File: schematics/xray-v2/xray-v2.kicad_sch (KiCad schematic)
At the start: 136 parts, among them J1 USB_B_Micro, J2 USB_A, J3 USB_C_Receptacle_USB2.0, J4 USBASP, M1 VibroMotor, 3V, 8x2.7mm, Q1 IRF7832PbF, Q10 IRLML5203, Q11 IRLML0030, Q12 IRLML0030, Q13 IRLML0030, Q14 IRLML0030, Q2 IRF7425PbF, Q3 IRLML0030, Q4 IRF7425PbF, Q7 BC847, Q8 IRLML0030, Q9 IRLML5203, SW1 EC11W****, SW2 B3F3150, SW3 SW_Push, T1 Transformer_1P_1S, U1 PCA9306, U2 IP5328P, U3 ATmega328P-A, U4 SN74LVC2T45DCUR, U5 SN74LVC2T45DCUR, U6 SN74LVC2T45DCUR, U7 Display_1.18inch_st7535, U8 AMS1117-3.3, U9 CP2102N-Axx-xQFN28, Y1 HC-49SM, 8MHz

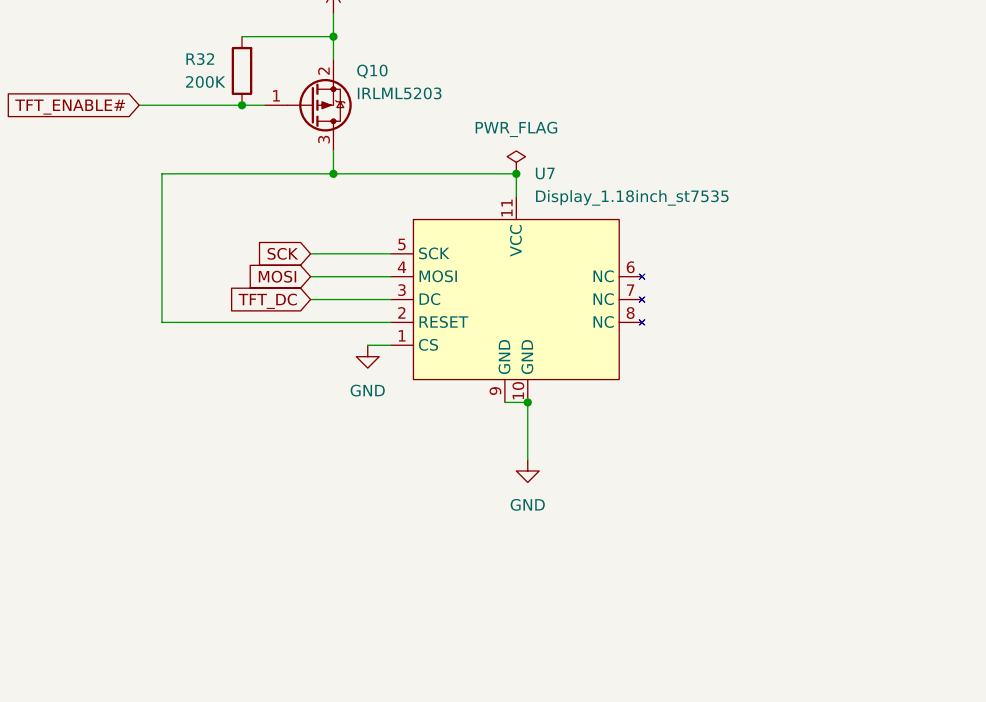
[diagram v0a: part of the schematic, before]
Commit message: Display changed 1.8'' -> 2.2''
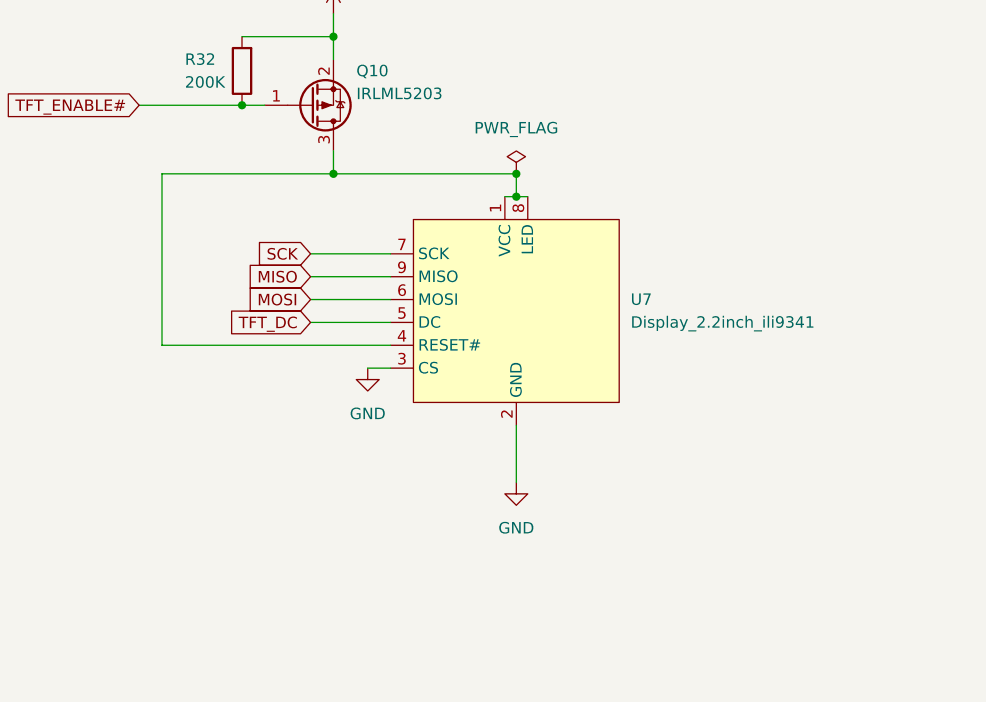
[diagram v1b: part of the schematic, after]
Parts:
- removed U7: Display_1.18inch_st7535, Library:Display_1.18inch_st7735, symbol My_Library:Display_1.18inch_st7535
- added U7: Display_2.2inch_ili9341, Library:Display_2.2inch_ili9341, symbol My_Library:Display_2.2inch_ili9341
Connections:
- net GND: now also U7.2 (GND), U7.3 (CS)
- net MISO: now also U7.9 (MISO)
- net MOSI: now also U7.6 (MOSI)
- net SCK: now also U7.7 (SCK)
- net TFT_DC: now also U7.5 (DC)
- net at Q10.3 (D): now also U7.1 (VCC), U7.4 (RESET#), U7.8 (LED)
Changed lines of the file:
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@@
   (junction (at 71.12 99.06) (diameter 0) (color 0 0 0 0)
   )
+  (junction (at 763.27 393.7) (diameter 0) (color 0 0 0 0)
+  )
   (junction (at 685.8 247.65) (diameter 0) (color 0 0 0 0)
   )
@@
   (junction (at 149.86 494.03) (diameter 0) (color 0 0 0 0)
   )
-  (junction (at 764.54 416.56) (diameter 0) (color 0 0 0 0)
-  )
   (junction (at 445.77 293.37) (diameter 0) (color 0 0 0 0)
   )
@@
     (stroke (width 0) (type default))
   )
-  (wire (pts (xy 749.3 405.13) (xy 740.41 405.13))
+  (wire (pts (xy 749.3 407.67) (xy 740.41 407.67))
     (stroke (width 0) (type default))
   )
@@
     (stroke (width 0) (type default))
   )
-  (wire (pts (xy 762 416.56) (xy 764.54 416.56))
-    (stroke (width 0) (type default))
-  )
   (wire (pts (xy 306.07 121.92) (xy 318.77 121.92))
     (stroke (width 0) (type default))
@@
     (stroke (width 0) (type default))
   )
-  (wire (pts (xy 764.54 416.56) (xy 764.54 422.91))
+  (wire (pts (xy 763.27 419.1) (xy 763.27 425.45))
     (stroke (width 0) (type default))
   )
@@
     (stroke (width 0) (type default))
   )
-  (wire (pts (xy 749.3 402.59) (xy 740.41 402.59))
+  (wire (pts (xy 749.3 405.13) (xy 740.41 405.13))
     (stroke (width 0) (type default))
   )
@@
     (stroke (width 0) (type default))
   )
+  (wire (pts (xy 763.27 393.7) (xy 764.54 393.7))
+    (stroke (width 0) (type default))
+  )
   (wire (pts (xy 659.13 241.3) (xy 659.13 247.65))
     (stroke (width 0) (type default))
@@
     (stroke (width 0) (type default))
   )
-  (wire (pts (xy 723.9 407.67) (xy 749.3 407.67))
-    (stroke (width 0) (type default))
-  )
   (wire (pts (xy 71.12 106.68) (xy 71.12 107.95))
     (stroke (width 0) (type default))
@@
     (stroke (width 0) (type default))
   )
+  (wire (pts (xy 749.3 402.59) (xy 740.41 402.59))
+    (stroke (width 0) (type default))
+  )
   (wire (pts (xy 121.92 483.87) (xy 125.73 483.87))
     (stroke (width 0) (type default))
@@
     (stroke (width 0) (type default))
   )
+  (wire (pts (xy 762 393.7) (xy 763.27 393.7))
+    (stroke (width 0) (type default))
+  )
   (wire (pts (xy 243.84 496.57) (xy 243.84 500.38))
     (stroke (width 0) (type default))
@@
     (stroke (width 0) (type default))
   )
-  (wire (pts (xy 746.76 410.21) (xy 749.3 410.21))
+  (wire (pts (xy 746.76 412.75) (xy 749.3 412.75))
     (stroke (width 0) (type default))
   )
@@
     (stroke (width 0) (type default))
   )
+  (wire (pts (xy 723.9 410.21) (xy 749.3 410.21))
+    (stroke (width 0) (type default))
+  )
   (wire (pts (xy 692.15 44.45) (xy 701.04 44.45))
     (stroke (width 0) (type default))
@@
     (stroke (width 0) (type default))
   )
-  (wire (pts (xy 723.9 407.67) (xy 723.9 391.16))
+  (wire (pts (xy 723.9 391.16) (xy 723.9 410.21))
     (stroke (width 0) (type default))
   )
@@
     )
   )
-  (global_label "MOSI" (shape input) (at 740.41 402.59 180) (fields_autoplaced)
+  (global_label "MOSI" (shape input) (at 740.41 405.13 180) (fields_autoplaced)
     (effects (font (size 1.27 1.27)) (justify right))
-    (property "Intersheetrefs" "${INTERSHEET_REFS}" (at 733.4007 402.5106 0)
+    (property "Intersheetrefs" "${INTERSHEET_REFS}" (at 733.4007 405.0506 0)
       (effects (font (size 1.27 1.27)) (justify right) hide)
     )
@@
     )
   )
-  (global_label "TFT_DC" (shape input) (at 740.41 405.13 180) (fields_autoplaced)
+  (global_label "TFT_DC" (shape input) (at 740.41 407.67 180) (fields_autoplaced)
     (effects (font (size 1.27 1.27)) (justify right))
-    (property "Intersheetrefs" "${INTERSHEET_REFS}" (at 731.4655 405.0506 0)
+    (property "Intersheetrefs" "${INTERSHEET_REFS}" (at 731.4655 407.5906 0)
       (effects (font (size 1.27 1.27)) (justify right) hide)
     )
@@
     )
   )
+  (global_label "MISO" (shape input) (at 740.41 402.59 180) (fields_autoplaced)
+    (effects (font (size 1.27 1.27)) (justify right))
+    (property "Intersheetrefs" "${INTERSHEET_REFS}" (at 732.8286 402.59 0)
+      (effects (font (size 1.27 1.27)) (justify right) hide)
+    )
+  )
   (global_label "USB_M_IN_VBUS_G" (shape input) (at 90.17 110.49 270) (fields_autoplaced)
     (effects (font (size 1.27 1.27)) (justify right))
@@
     )
   )
+  (symbol (lib_id "My_Library:Display_2.2inch_ili9341") (at 763.27 407.67 0) (unit 1)
+    (in_bom yes) (on_board yes) (dnp no) (fields_autoplaced)
+    (property "Reference" "U7" (at 775.97 405.13 0)
+      (effects (font (size 1.27 1.27)) (justify left))
+    )
+    (property "Value" "Display_2.2inch_ili9341" (at 775.97 407.67 0)
+      (effects (font (size 1.27 1.27)) (justify left))
+    )
+    (property "Footprint" "Library:Display_2.2inch_ili9341" (at 763.27 407.67 0)
+      (effects (font (size 1.27 1.27)) hide)
+    )
+    (property "Datasheet" "" (at 763.27 407.67 0)
+      (effects (font (size 1.27 1.27)) hide)
+    )
+    (pin "1")
+    (pin "2")
+    (pin "3")
+    (pin "4")
+    (pin "5")
+    (pin "6")
+    (pin "7")
+    (pin "8")
+    (pin "9")
+    (instances
+      (project "xray-v2"
+        (path "/41c926b9-3ecb-4e5f-9a53-cebe2d97cbdc"
+          (reference "U7") (unit 1)
+        )
+      )
+    )
+  )
   (symbol (lib_id "power:GND") (at 231.14 81.28 0) (unit 1)
     (in_bom yes) (on_board yes) (dnp no) (fields_autoplaced)
@@
     )
   )
-  (symbol (lib_id "My_Library:Display_1.18inch_st7535") (at 763.27 405.13 0) (unit 1)
-    (in_bom yes) (on_board yes) (dnp no) (fields_autoplaced)
-    (property "Reference" "U7" (at 765.2894 391.16 0)
-      (effects (font (size 1.27 1.27)) (justify left))
-    )
-    (property "Value" "Display_1.18inch_st7535" (at 765.2894 393.7 0)
-      (effects (font (size 1.27 1.27)) (justify left))
-    )
-    (property "Footprint" "Library:Display_1.18inch_st7735" (at 763.27 405.13 0)
-      (effects (font (size 1.27 1.27)) hide)
-    )
-    (property "Datasheet" "" (at 763.27 405.13 0)
-      (effects (font (size 1.27 1.27)) hide)
-    )
-    (pin "1")
-    (pin "10")
-    (pin "11")
-    (pin "2")
-    (pin "3")
-    (pin "4")
-    (pin "5")
-    (pin "6")
-    (pin "7")
-    (pin "8")
-    (pin "9")
-    (instances
-      (project "xray"
-        (path "/002cc585-3681-421a-8dca-b0910197d82b"
-          (reference "U7") (unit 1)
-        )
-      )
-      (project "xray-v2"
-        (path "/41c926b9-3ecb-4e5f-9a53-cebe2d97cbdc"
-          (reference "U7") (unit 1)
-        )
-      )
-    )
-  )
   (symbol (lib_id "power:GND") (at 153.67 293.37 0) (unit 1)
     (in_bom yes) (on_board yes) (dnp no) (fields_autoplaced)
@@
     )
   )
-  (symbol (lib_id "power:GND") (at 746.76 410.21 0) (unit 1)
+  (symbol (lib_id "power:GND") (at 746.76 412.75 0) (unit 1)
     (in_bom yes) (on_board yes) (dnp no) (fields_autoplaced)
-    (property "Reference" "#PWR069" (at 746.76 416.56 0)
+    (property "Reference" "#PWR069" (at 746.76 419.1 0)
       (effects (font (size 1.27 1.27)) hide)
     )
-    (property "Value" "GND" (at 746.76 415.29 0)
+    (property "Value" "GND" (at 746.76 417.83 0)
       (effects (font (size 1.27 1.27)))
     )
-    (property "Footprint" "" (at 746.76 410.21 0)
+    (property "Footprint" "" (at 746.76 412.75 0)
       (effects (font (size 1.27 1.27)) hide)
     )
-    (property "Datasheet" "" (at 746.76 410.21 0)
+    (property "Datasheet" "" (at 746.76 412.75 0)
       (effects (font (size 1.27 1.27)) hide)
     )
@@
     )
   )
-  (symbol (lib_id "power:GND") (at 764.54 422.91 0) (unit 1)
+  (symbol (lib_id "power:GND") (at 763.27 425.45 0) (unit 1)
     (in_bom yes) (on_board yes) (dnp no) (fields_autoplaced)
-    (property "Reference" "#PWR073" (at 764.54 429.26 0)
+    (property "Reference" "#PWR073" (at 763.27 431.8 0)
       (effects (font (size 1.27 1.27)) hide)
     )
-    (property "Value" "GND" (at 764.54 427.99 0)
+    (property "Value" "GND" (at 763.27 430.53 0)
       (effects (font (size 1.27 1.27)))
     )
-    (property "Footprint" "" (at 764.54 422.91 0)
+    (property "Footprint" "" (at 763.27 425.45 0)
       (effects (font (size 1.27 1.27)) hide)
     )
-    (property "Datasheet" "" (at 764.54 422.91 0)
+    (property "Datasheet" "" (at 763.27 425.45 0)
       (effects (font (size 1.27 1.27)) hide)
     )

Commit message: changed usb-flush schematics
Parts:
- removed C25: 100 nF, Capacitor_SMD:C_0603_1608Metric, symbol Device:C
- removed H3: MountingHole, MountingHole:MountingHole_2.2mm_M2, symbol Mechanical:MountingHole
- added JP2: USBF_EN, Jumper:SolderJumper-2_P1.3mm_Open_TrianglePad1.0x1.5mm, symbol Jumper:SolderJumper_2_Open
- added R15: 10K, Resistor_SMD:R_0805_2012Metric, symbol Device:R
- added TP2: UV_PWM, TestPoint:TestPoint_Pad_1.0x1.0mm, symbol Connector:TestPoint
- added TP3: L_PWM, TestPoint:TestPoint_Pad_1.0x1.0mm, symbol Connector:TestPoint
- added TP4: VREG, TestPoint:TestPoint_Pad_1.0x1.0mm, symbol Connector:TestPoint
- added TP5: VMID, TestPoint:TestPoint_Pad_1.0x1.0mm, symbol Connector:TestPoint
- JP1: renamed from JP2; value Jumper_2_Open -> UV_EN
- JP3: value SolderJumper_2_Open -> USBF_RST_EN
- R15: value 10K -> 1K
- renumbered C34 to C3, C41 to C5, R18 to R4, SW3 to SW1, U8 to U1, U9 to U2, U7 to U9, V2 to V1
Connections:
- net +5V: now also JP2.1 (A)
- net FLUSH_VBUS: now also JP2.2 (B)
- net GND: now also R15.1
- net RXD: no longer U2.26 (TXD)
- net TXD: no longer U2.25 (RXD)
- net USB_VMID: now also TP5.1
- net UV_PWM: now also TP2.1
- net VREG: now also TP4.1
- net at U2.11 (~{SUSPEND}): now also R15.2
- net at C18.2, L1.2, U2.14 (LX_1)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: now also TP3.1
- net RXD_5V: now reaches J4.4 (Pin_4), U4.7 (B1)
- net RXD_5V: now also U2.26 (TXD)
- net TXD_5V: now reaches J4.6 (Pin_6), U6.6 (B2)
- net TXD_5V: now also U2.25 (RXD)
- no-connect marks 27 -> 26
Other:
- moved on the sheet: H3, J1, R15

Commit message: Board v2 ordered. Preparing firmware to work with board-v2
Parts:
- added D2: BZV55C3V9, Diode_SMD:D_MiniMELF, symbol Diode:BZV55C3V9
- added D5: SMAJ5.0CA-TR, Diode_SMD:D_SMA, symbol Diode:ESD9B3.3ST5G
- SW2: Поле4 (none) -> Display ON-OFF / Reset MCU
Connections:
- net CP2102_VREG: now also JP2.2 (B), D2.1 (K)
- net FLUSH_VBUS: now also D5.2 (A2); no longer JP2.2 (B)
- net GND: now also D2.2 (A), D5.1 (A1)
- net RXD_5V renamed RXD_V
- net TXD_5V renamed TXD_V
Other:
- moved on the sheet: JP2

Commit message: prepare to rewrite UI
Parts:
- R1: value 100 -> 510
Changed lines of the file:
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@@
       (effects (font (size 1.27 1.27)) (justify right))
     )
-    (property "Value" "100" (at 246.38 494.03 0)
+    (property "Value" "510" (at 246.38 494.03 0)
       (effects (font (size 1.27 1.27)) (justify right))
     )

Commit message: hardware works, printing box
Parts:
- removed D2: BZV55C3V9, Diode_SMD:D_MiniMELF, symbol Diode:BZV55C3V9
- removed D5: SMAJ5.0CA-TR, Diode_SMD:D_SMA, symbol Diode:ESD9B3.3ST5G
- removed JP1: SolderJumper_2_Open, Jumper:SolderJumper-2_P1.3mm_Open_TrianglePad1.0x1.5mm, symbol Jumper:SolderJumper_2_Open
- removed JP2: USBF_EN, Jumper:SolderJumper-2_P1.3mm_Open_TrianglePad1.0x1.5mm, symbol Jumper:SolderJumper_2_Open
- removed U1: AMS1117-3.3, Package_TO_SOT_SMD:SOT-223-3_TabPin2, symbol Regulator_Linear:AMS1117-3.3
- added C11: К73-17, 0.1 uF, 630V, Capacitor_THT:C_Rect_L16.5mm_W7.0mm_P15.00mm_MKT, symbol Device:C
- added C25: 100 nF, Capacitor_SMD:C_0603_1608Metric, symbol Device:C
- added D1: 15MQ030NPBF, Diode_SMD:D_SMA, symbol Device:D
- added D16 (x4): BAV21WS, Diode_SMD:D_SOD-323F, symbol Device:D
- added D2: SP0503BAHT, Package_TO_SOT_SMD:SOT-143, symbol Power_Protection:SP0503BAHT
- added D2: US1M, Diode_SMD:D_SMA, symbol Diode:US1M
- added D3: MBR0520, Diode_SMD:D_SOD-123, symbol Diode:MBR0520
- added JP3: FL_SPI_EN, Jumper:SolderJumper-2_P1.3mm_Open_TrianglePad1.0x1.5mm, symbol Jumper:SolderJumper_2_Open
- added R20, R32 (x3): 5K1, Resistor_SMD:R_0805_2012Metric, symbol Device:R
- added TP2: UV_STAB, TestPoint:TestPoint_Pad_1.0x1.0mm, symbol Connector:TestPoint
- added U1: XC6206P282MR, Package_TO_SOT_SMD:SOT-23-3, symbol Regulator_Linear:XC6206PxxxMR
- C11, C8, C9: footprint Capacitor_THT:C_Rect_L16.5mm_W9.0mm_P15.00mm_MKT -> Capacitor_THT:C_Rect_L16.5mm_W7.0mm_P15.00mm_MKT
- R1: value 10K -> 91K
- TP1: footprint TestPoint:TestPoint_Plated_Hole_D2.0mm -> TestPoint:TestPoint_Loop_D2.54mm_Drill1.5mm_Beaded
- renumbered JP3 to JP2, TP2 to TP3, TP3 to TP4, TP4 to TP5, TP5 to TP6
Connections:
- net +5V: now also D3.1 (K), JP3.2 (B), R20.2; no longer U5.8 (VCCB)
- net CP2102_VREG: now also D3.2 (A)
- net FLUSH_D+: now also D2.3 (K)
- net FLUSH_D-: now also D2.4 (K)
- net FLUSH_VBUS: now also D1.2 (A), D2.2 (K)
- net GND: now also C9.1, D2.2 (A), D2.1 (A), R32.2, R32.2, R32.2, U1.1 (GND); no longer C9.2
- net MISO: no longer U9.9 (MISO)
- net MOSI: now also U5.2 (A1), D16.2 (A); no longer U4.3 (A2), U9.6 (MOSI)
- net RESET: now also U4.2 (A1); no longer JP2.2 (B), U5.2 (A1)
- net RXD: now also U4.3 (A2); no longer U4.2 (A1)
- net RXD_V: now also U4.6 (B2); no longer U4.7 (B1)
- net SCK: now also D16.2 (A); no longer U9.7 (SCK)
- net TFT_DC: now also D16.2 (A); no longer U9.5 (DC)
- net USB_M_IN_VBUS: now also D1.1 (K)
- net DISPLAY_VCC: now reaches Q10.3 (D), U9.1 (VCC), U9.8 (LED)
- net DISPLAY_VCC: now also D16.2 (A); no longer U9.4 (RESET#)
- net at C3.1, Q9.3 (D): now also U1.3 (VI)
- net at C5.1, R4.1: now also TP2.1, U1.2 (VO)
- net at J4.1 (Pin_1): now also U5.7 (B1); no longer U4.6 (B2)
- net at C11.2, D3.1 (K), R1.2: now also R10.1
- net RESET_V: now reaches J4.5 (Pin_5)
- net RESET_V: now also U4.7 (B1), C25.2, R20.1; no longer U5.7 (B1)
- new net: D16.1 (K), U9.4 (RESET#)
- new net: D16.1 (K), R32.1, U9.5 (DC)
- new net: D16.1 (K), R32.1, U9.6 (MOSI)
- new net: D16.1 (K), R32.1, U9.7 (SCK)
- new net: C11.1, C8.2, T1.4 (SB)
- new net: C11.2, D1.1 (K), D3.2 (A)
- new net: C9.2, D1.2 (A), D2.1 (K)
- new net: C8.1, D2.1 (K), D2.2 (A)
- new net: JP3.1 (A), U5.8 (VCCB)
- new net: C25.1, JP2.2 (B)
- no-connect marks 26 -> 27
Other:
- note added: "+"
- note added: "+ 1U -"
- note added: "-"
- note added: "- 3U +"
- note added: "2U"
- note added: "4U"
- moved on the sheet: C11, C24, C8, C9, D1, D2, D3, Q10, Q7, R1, R10, R11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

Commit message: v3
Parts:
- renumbered C25 to C1, C25 to C10, C10 to C11, C8 to C13, C13 to C14, C25 to C15, C9 to C16, C15 to C17, C11 to C18, C16 to C19, C25 to C2, C11 to C20, C18 to C21, C19 to C22, C20 to C23, C21 to C24, C22 to C25, C25 to C26, C25 to C27, C27 to C28, C32 to C30, C33 to C31, C14 to C32, C24 to C33, C17 to C34, C23 to C35, C28 to C36, C30 to C37, C31 to C38, C7 to C39, C25 to C4, C38 to C40, C35 to C41, C36 to C42, C37 to C43, C40 to C44, C39 to C45, C1 to C6, C5 to C7, C25 to C8, C6 to C9, D16 to D10, D16 to D11, D16 to D12, D16 to D13, D1 to D14, D2 to D4, D2 to D5, D1 to D6, D3 to D7, D4 to D8, D6 to D9, H3 to H2, H3 to H4, H3 to H5, H3 to H6, H3 to H7, J1 to J2, J2 to J3, J3 to J4, J4 to J5, Q9 to Q1, Q14 to Q11, Q9 to Q12, Q12 to Q13, Q13 to Q14, Q1 to Q2, Q2 to Q3, Q3 to Q5, Q7 to Q6, Q9 to Q7, Q11 to Q8, Q8 to Q9, R1 to R10, R15 to R11, R10 to R12, R16 to R13, R11 to R14, R12 to R15, R19 to R16, R13 to R17, R14 to R18, R24 to R19, R5 to R2, R23 to R20, R25 to R21, R20 to R22, R2 to R23, R3 to R24, R20 to R25, R7 to R26, R30 to R27, R31 to R28, R27 to R29, R6 to R3, R26 to R30, R32 to R31, R29 to R32, R32 to R33, R32 to R34, R32 to R35, R33 to R36, R34 to R37, R35 to R38, R31 to R39, R4 to R5, R15 to R6, R15 to R7, SW1 to SW3, U2 to U3, U3 to U4, U4 to U5, U5 to U6, U6 to U7, U1 to U8
